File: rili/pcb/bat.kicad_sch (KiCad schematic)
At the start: 21 parts, among them J10 Battery, Q2 AO3407, Q4 FS8205, SW54 SW_SPDT, U18 TP4056-42-ESOP8, U20 HT7833, U23 DW01A

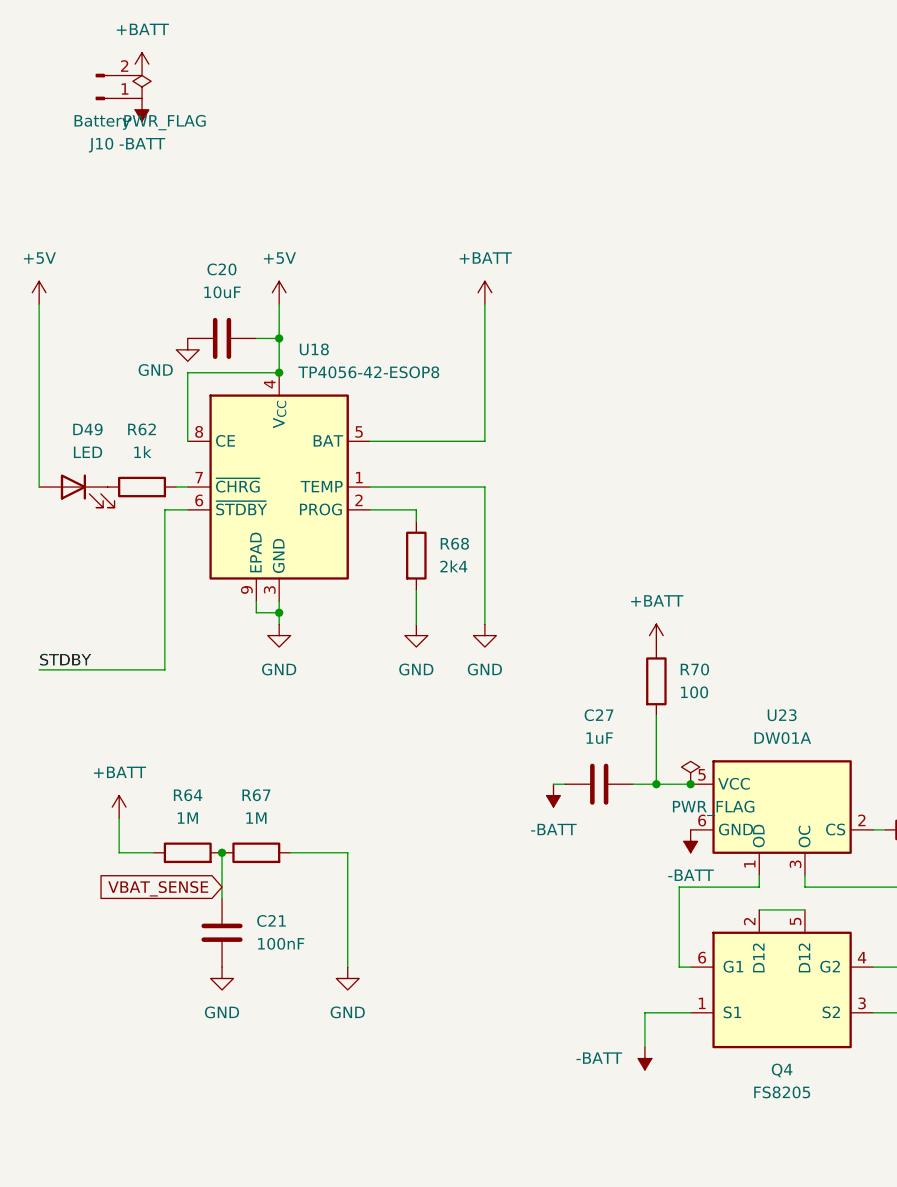
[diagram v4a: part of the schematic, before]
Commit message: review : solde complet — Tip TRRS protégé, condos +BATT, prog P4 dégagée
- TVS Tip : canal 3 des SRV05 relié au Tip des deux jacks (net TIP_5V, validé
  netlist : jack.T + load switch OUT + SRV05 sans toucher LINK_5V_EN)
- C29/C30 : 10µF sur +BATT/+BATT_D près des TP4056, placés et routés par Mae
- R48/R49 supprimés par Mae (CH334R : pull-up RESET# interne 25k, mode
  sans-quartz XO flottant conforme datasheet, fuite batterie→hub éliminée)
- pistes JP1/JP2 (prog USB du P4) écartées de la zone GND : zéro violation
- nettoyage : no_connect orpheline de la dépose R48/R49
- DRC 36/26 → 17/22 (ménage de routage par Mae), ratchet enregistré

Décisions documentées : SD manipulée hors tension (pas de TVS SD), tables de
pins matrice réelles + conventions firmware en annexe du plan v2.

Co-Authored-By: Claude Fable 5 <noreply@anthropic.com>
Claude-Session: https://claude.ai/code/session_01GfX5RmekmQi78Dm37qsT4Z
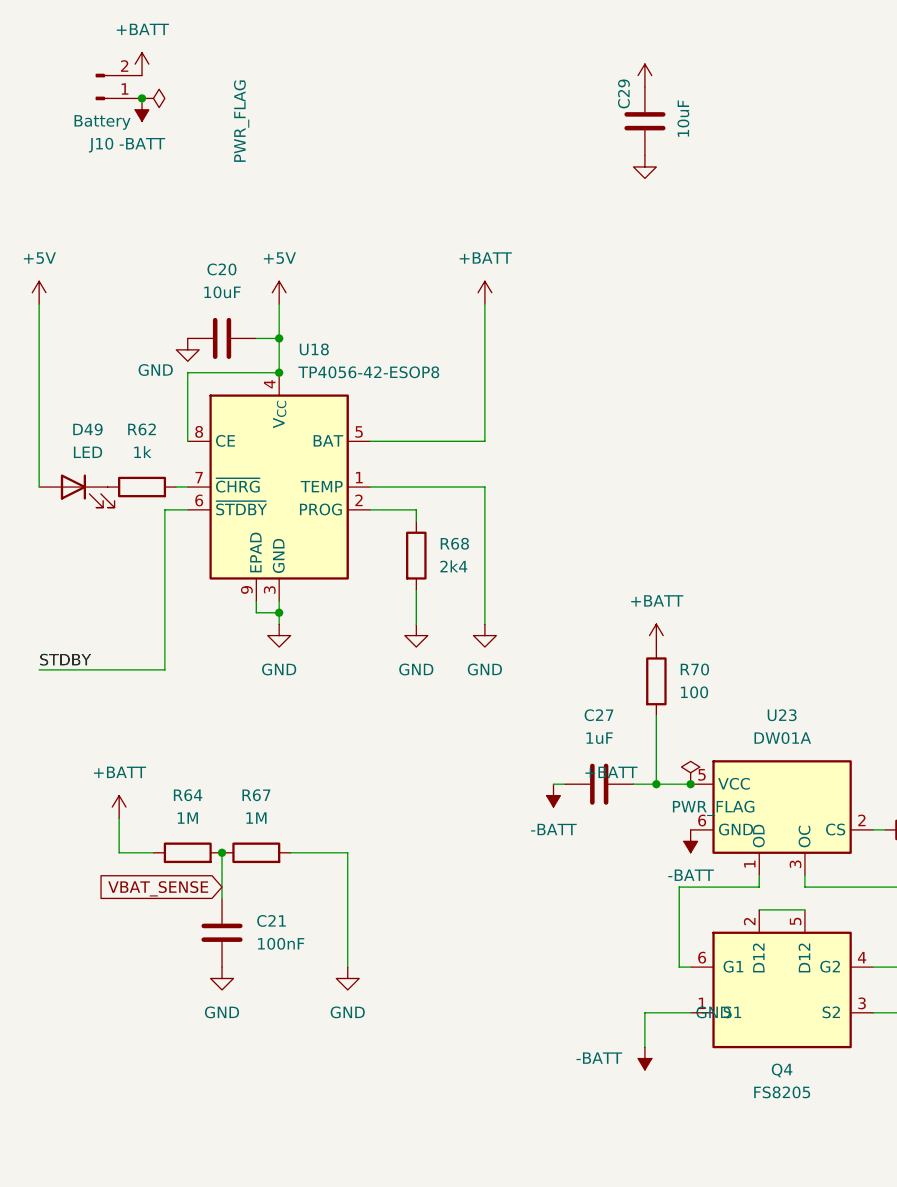
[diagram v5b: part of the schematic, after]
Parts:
- added C29: 10uF, Capacitor_SMD:C_1206_3216Metric_Pad1.33x1.80mm_HandSolder, symbol Device:C
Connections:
- net +BATT: now also C29.1
- net GND: now also C29.2
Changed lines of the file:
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@@
 	)
 	(junction
+		(at 31.75 24.13)
+		(diameter 0)
+		(color 0 0 0 0)
+	)
+	(junction
 		(at 69.85 170.18)
 		(diameter 0)
@@
 	)
 	(symbol
+		(lib_id "power:+BATT")
+		(at 87.63 22.86 0)
+		(unit 1)
+		(body_style 1)
+		(exclude_from_sim no)
+		(in_bom yes)
+		(on_board yes)
+		(in_pos_files yes)
+		(dnp no)
+		(fields_autoplaced yes)
+		(property "Reference" "#PWR0922"
+			(at 83.82 107.95 0)
+			(hide yes)
+			(show_name no)
+			(do_not_autoplace no)
+			(effects
+				(font
+					(size 1.27 1.27)
+				)
+			)
+		)
+		(property "Value" "+BATT"
+			(at 83.82 99.06 0)
+			(show_name no)
+			(do_not_autoplace no)
+			(effects
+				(font
+					(size 1.27 1.27)
+				)
+			)
+		)
+		(property "Footprint" ""
+			(at 83.82 104.14 0)
+			(hide yes)
+			(show_name no)
+			(do_not_autoplace no)
+			(effects
+				(font
+					(size 1.27 1.27)
+				)
+			)
+		)
+		(property "Datasheet" ""
+			(at 83.82 104.14 0)
+			(hide yes)
+			(show_name no)
+			(do_not_autoplace no)
+			(effects
+				(font
+					(size 1.27 1.27)
+				)
+			)
+		)
+		(property "Description" "Power symbol creates a global label with name \"+BATT\""
+			(at 83.82 104.14 0)
+			(hide yes)
+			(show_name no)
+			(do_not_autoplace no)
+			(effects
+				(font
+					(size 1.27 1.27)
+				)
+			)
+		)
+		(pin "1"
+		)
+		(instances
+			(project "niphar"
+				(path "/7138aad8-3c5f-41d0-9987-adc2f08f0576/d1dace0b-a9b6-45b3-8b77-6cc73528f4f2"
+					(reference "#PWR0922")
+					(unit 1)
+				)
+			)
+		)
+	)
+	(symbol
 		(lib_id "power:PWR_FLAG")
 		(at 78.74 170.18 0)
@@
 	(symbol
 		(lib_id "power:PWR_FLAG")
-		(at 31.75 24.13 0)
+		(at 31.75 24.13 270)
 		(unit 1)
 		(body_style 1)
@@
 		(dnp no)
 		(property "Reference" "#FLG03"
-			(at 34.29 24.13 0)
+			(at 31.75 26.67 0)
 			(hide yes)
 			(show_name no)
@@
 		)
 		(property "Value" "PWR_FLAG"
-			(at 34.29 26.67 0)
+			(at 42.672 26.67 0)
 			(show_name no)
 			(do_not_autoplace no)
@@
 	)
 	(symbol
+		(lib_id "Device:C")
+		(at 87.63 26.67 0)
+		(unit 1)
+		(body_style 1)
+		(exclude_from_sim no)
+		(in_bom yes)
+		(on_board yes)
+		(in_pos_files yes)
+		(dnp no)
+		(property "Reference" "C29"
+			(at 85.344 23.622 90)
+			(show_name no)
+			(do_not_autoplace no)
+			(effects
+				(font
+					(size 1.27 1.27)
+				)
+			)
+		)
+		(property "Value" "10uF"
+			(at 91.948 26.416 90)
+			(show_name no)
+			(do_not_autoplace no)
+			(effects
+				(font
+					(size 1.27 1.27)
+				)
+			)
+		)
+		(property "Footprint" "Capacitor_SMD:C_1206_3216Metric_Pad1.33x1.80mm_HandSolder"
+			(at 99.06 49.8348 0)
+			(hide yes)
+			(show_name no)
+			(do_not_autoplace no)
+			(effects
+				(font
+					(size 1.27 1.27)
+				)
+			)
+		)
+		(property "Datasheet" ""
+			(at 95.25 50.8 0)
+			(hide yes)
+			(show_name no)
+			(do_not_autoplace no)
+			(effects
+				(font
+					(size 1.27 1.27)
+				)
+			)
+		)
+		(property "Description" "Unpolarized capacitor"
+			(at 95.25 50.8 0)
+			(hide yes)
+			(show_name no)
+			(do_not_autoplace no)
+			(effects
+				(font
+					(size 1.27 1.27)
+				)
+			)
+		)
+		(pin "2"
+		)
+		(pin "1"
+		)
+		(instances
+			(project "niphar"
+				(path "/7138aad8-3c5f-41d0-9987-adc2f08f0576/d1dace0b-a9b6-45b3-8b77-6cc73528f4f2"
+					(reference "C29")
+					(unit 1)
+				)
+			)
+		)
+	)
+	(symbol
 		(lib_id "power:+BATT")
 		(at 69.85 46.99 0)
@@
 					(unit 1)
 				)
+			)
+		)
+	)
+	(symbol
+		(lib_id "power:GND")
+		(at 87.63 30.48 0)
+		(unit 1)
+		(body_style 1)
+		(exclude_from_sim no)
+		(in_bom yes)
+		(on_board yes)
+		(in_pos_files yes)
+		(dnp no)
+		(fields_autoplaced yes)
+		(property "Reference" "#PWR0923"
+			(at 95.25 127 0)
+			(hide yes)
+			(show_name no)
+			(do_not_autoplace no)
+			(effects
+				(font
+					(size 1.27 1.27)
+				)
+			)
+		)
+		(property "Value" "GND"
+			(at 95.25 125.73 0)
+			(show_name no)
+			(do_not_autoplace no)
+			(effects
+				(font
+					(size 1.27 1.27)
+				)
+			)
+		)
+		(property "Footprint" ""
+			(at 95.25 120.65 0)
+			(hide yes)
+			(show_name no)
+			(do_not_autoplace no)
+			(effects
+				(font
+					(size 1.27 1.27)
+				)
+			)
+		)
+		(property "Datasheet" ""
+			(at 95.25 120.65 0)
+			(hide yes)
+			(show_name no)
+			(do_not_autoplace no)
+			(effects
+				(font
+					(size 1.27 1.27)
+				)
+			)
+		)
+		(property "Description" "Power symbol creates a global label with name \"GND\" , ground"
+			(at 95.25 120.65 0)
+			(hide yes)
+			(show_name no)
+			(do_not_autoplace no)
+			(effects
+				(font
+					(size 1.27 1.27)
+				)
+			)
+		)
+		(pin "1"
+		)
+		(instances
+			(project "niphar"
+				(path "/7138aad8-3c5f-41d0-9987-adc2f08f0576/d1dace0b-a9b6-45b3-8b77-6cc73528f4f2"
+					(reference "#PWR0923")
+					(unit 1)
+				)
